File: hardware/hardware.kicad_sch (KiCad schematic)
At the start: 34 parts, among them J2 Conn_01x03, Q1 AON6500, Q2 AON6500, Q3 AON6500, Q4 AON6500, Q5 AON6500, Q6 AON6500, U1 CH32M007G8R6

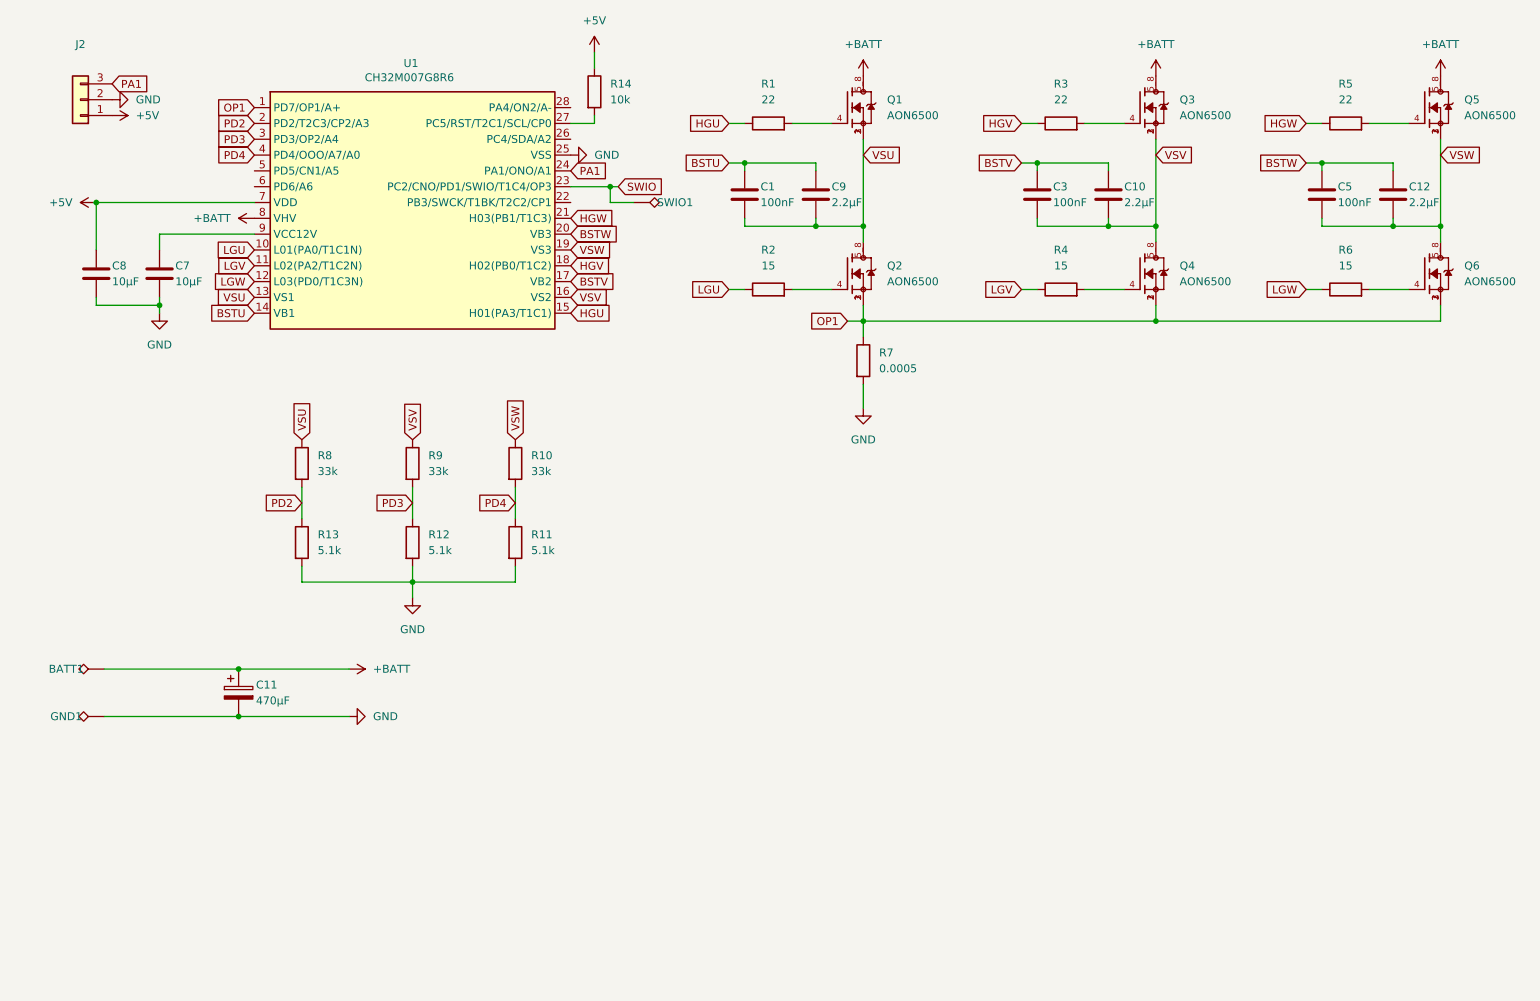
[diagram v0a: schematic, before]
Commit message: use AOD514 instead AON6400
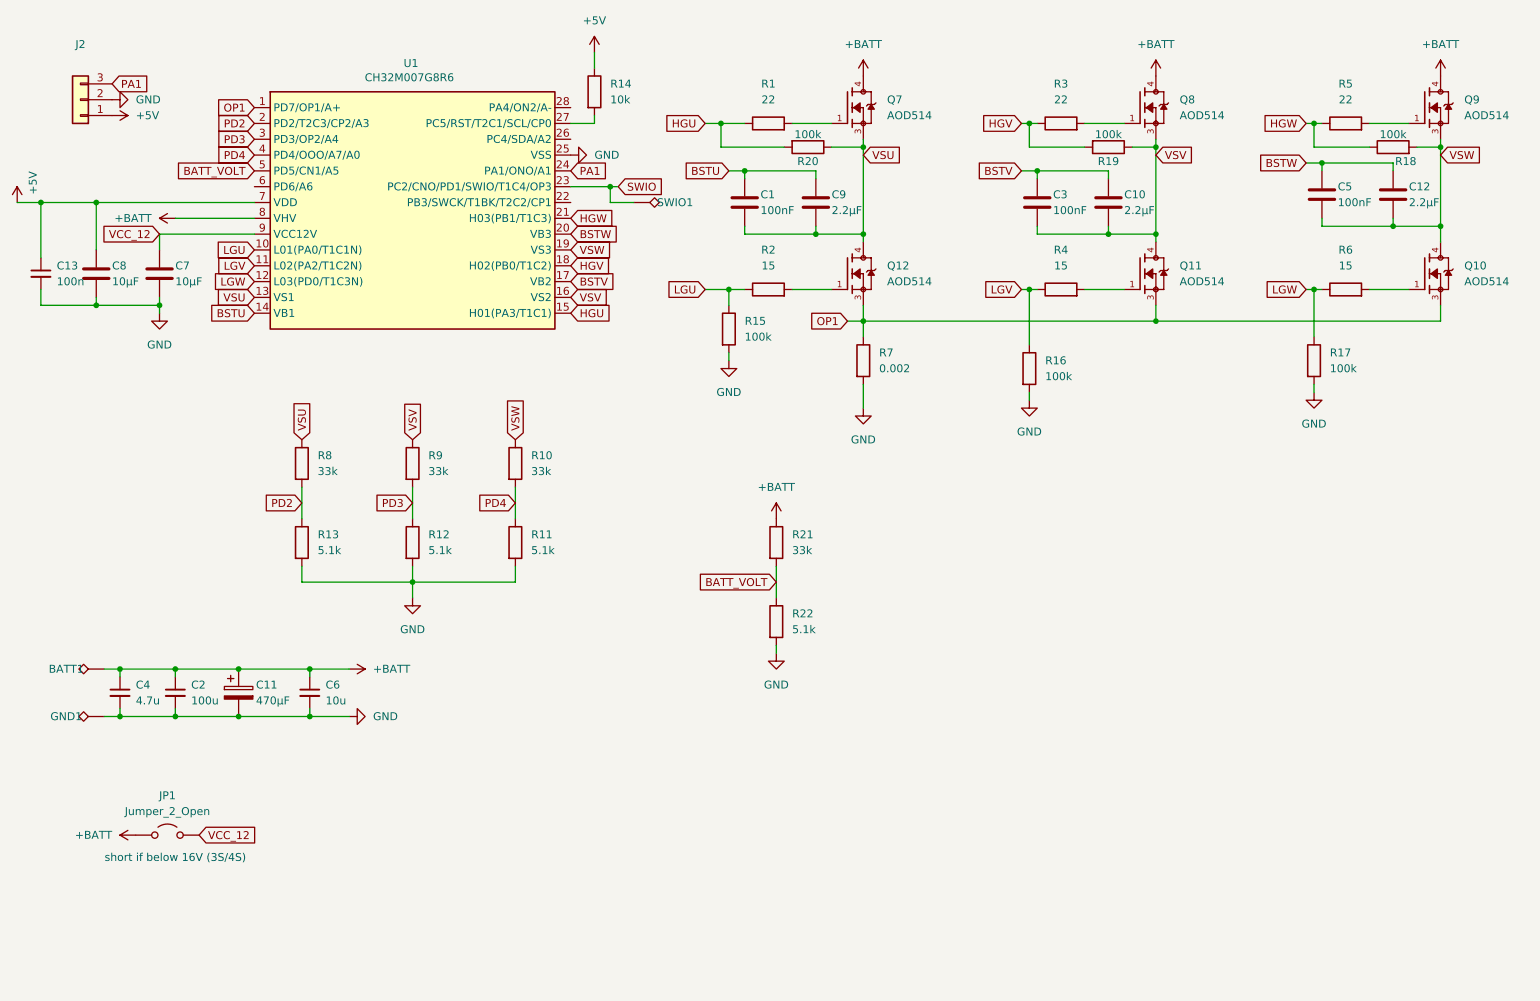
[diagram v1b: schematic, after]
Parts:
- removed Q1, Q2, Q3, Q4, Q5, Q6: AON6500, AON6500:TRANS_AON6500, symbol AON6500:AON6500
- added C13: 100n, Capacitor_SMD:C_0805_2012Metric, symbol Device:C_Small
- added C2: 100u, Capacitor_SMD:C_1206_3216Metric, symbol Device:C_Small
- added C4: 4.7u, Capacitor_SMD:C_0805_2012Metric, symbol Device:C_Small
- added C6: 10u, Capacitor_SMD:C_0805_2012Metric, symbol Device:C_Small
- added JP1: Jumper_2_Open, Jumper:SolderJumper-2_P1.3mm_Open_TrianglePad1.0x1.5mm, symbol Jumper:Jumper_2_Open
- added Q10, Q11, Q12, Q7, Q8, Q9: AOD514, AOD514:TRANS_AOD514, symbol AOD514:AOD514
- added R15, R16, R17, R18, R19, R20: 100k, Resistor_SMD:R_0603_1608Metric, symbol Device:R
- added R21: 33k, Resistor_SMD:R_0603_1608Metric, symbol Device:R
- added R22: 5.1k, Resistor_SMD:R_0603_1608Metric, symbol Device:R
- R7: value 0.0005 -> 0.002
- U1: footprint Package_SO:TSSOP-28_4.4x9.7mm_P0.65mm -> Package_SO:SSOP-28_3.9x9.9mm_P0.635mm
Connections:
- net +5V: now also C13.1
- net +BATT: now also C2.1, C4.1, C6.1, JP1.1 (A), Q7.4, Q8.4, Q9.4, R21.1
- net GND: now also C13.2, C2.2, C4.2, C6.2, R15.2, R16.2, R17.2, R22.2
- net HGU: now also R20.2
- net HGV: now also R19.2
- net HGW: now also R18.1
- net LGU: now also R15.1
- net LGV: now also R16.1
- net LGW: now also R17.1
- net OP1: now also Q10.3, Q11.3, Q12.3
- net VSU: now also Q12.4, Q7.3, R20.1
- net VSV: now also Q11.4, Q8.3, R19.1
- net VSW: now also Q10.4, Q9.3, R18.2
- net at R4.2: now also Q11.1
- net at R3.2: now also Q8.1
- net at R6.2: now also Q10.1
- net at R2.2: now also Q12.1
- net at R1.2: now also Q7.1
- net at R5.2: now also Q9.1
- net VCC_12: now reaches C7.2, U1.9 (VCC12V)
- net VCC_12: now also JP1.2 (B)
- net BATT_VOLT: now reaches U1.5 (PD5/CN1/A5)
- net BATT_VOLT: now also R21.2, R22.1
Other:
- note added: "short if below 16V (3S/4S)"
- moved on the sheet: C1, C10, C3, C9

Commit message: add shunt A- + led + ntc
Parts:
- added D1: BLUE, LED_SMD:LED_0603_1608Metric, symbol Device:LED
- added R24: 10k, Resistor_SMD:R_0603_1608Metric, symbol Device:R
- added R25: 1.1k, Resistor_SMD:R_0603_1608Metric, symbol Device:R
- added TH1: NTC 10k B3950, Capacitor_SMD:C_0603_1608Metric, symbol Device:Thermistor_NTC
- C2: value 100u -> 100n
- R11, R12, R13, R22: value 5.1k -> 8,2k
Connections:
- net +5V: now also TH1.1
- net GND: now also U1.28 (PA4/ON2/A-), R24.2, R25.2
- net LED: now reaches U1.26 (PC4/SDA/A2)
- net LED: now also D1.2 (A)
- net NTC: now reaches U1.6 (PD6/A6)
- net NTC: now also R24.1, TH1.2
- new net: D1.1 (K), R25.1
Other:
- note added: "4S Maximum"
- moved on the sheet: BATT1, C11, C2, C4, C6, GND1, R14, R7

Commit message: first pcb position
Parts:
- removed BATT1, GND1: TestPoint_Alt, TestPoint:TestPoint_Pad_3.0x3.0mm, symbol Connector:TestPoint_Alt
- added J1: AMASS, Connector_AMASS:AMASS_XT60-F_1x02_P7.20mm_Vertical, symbol Connector_Generic:Conn_01x02
- added VSU1, VSV1, VSW1: TestPoint_Alt, TestPoint:TestPoint_Pad_3.0x3.0mm, symbol Connector:TestPoint_Alt
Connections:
- net +BATT: now also J1.2 (Pin_2)
- net GND: now also J1.1 (Pin_1)
- net VSU: now also VSU1.1
- net VSV: now also VSV1.1
- net VSW: now also VSW1.1

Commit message: finish pcb wiring + change batt+ capacitors
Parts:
- removed C11: 470µF, Capacitor_THT:CP_Radial_D10.0mm_P5.00mm, symbol Device:C_Polarized
- added C11, C14, C15: 100n, Capacitor_SMD:C_1206_3216Metric, symbol Device:C_Small
- J1: footprint Connector_AMASS:AMASS_XT60-F_1x02_P7.20mm_Vertical -> Connector_AMASS:AMASS_XT30PW-F_1x02_P2.50mm_Horizontal
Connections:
- net +BATT: now also C11.1, C14.1, C15.1
- net GND: now also C11.2, C14.2, C15.2; no longer U1.28 (PA4/ON2/A-)
- new net A-: U1.28 (PA4/ON2/A-)
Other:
- moved on the sheet: C6

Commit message: add revision + finish PCB
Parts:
- J1: footprint Connector_AMASS:AMASS_XT30PW-F_1x02_P2.50mm_Horizontal -> Connector_AMASS:AMASS_XT30U-F_1x02_P5.0mm_Vertical
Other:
- company: (none) -> Rmingon
- title: (none) -> Cogless
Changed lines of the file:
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@@
 	(generator_version "10.0")
 	(paper "A4")
+	(title_block
+		(title "Cogless")
+		(date "2026-08-16")
+		(rev "V0.1")
+		(company "Rmingon")
+	)
 	(text "4S Maximum"
 		(exclude_from_sim no)
@@
 			)
 		)
-		(property "Footprint" "Connector_AMASS:AMASS_XT30PW-F_1x02_P2.50mm_Horizontal"
+		(property "Footprint" "Connector_AMASS:AMASS_XT30U-F_1x02_P5.0mm_Vertical"
 			(at 21.59 165.1 0)
 			(hide yes)
